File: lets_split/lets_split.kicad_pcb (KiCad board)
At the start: 2 copper layers, 111.8 x 79 mm, 69 parts, among them J1 3PIN, J2 6PIN, J3 3PIN, J4 3PIN, J5 3PIN, M1 FIDUCIAL, M2 FIDUCIAL, M3 FIDUCIAL, M4 FIDUCIAL, SW1 SW_PUSH, SW10 SW_PUSH, SW11 SW_PUSH, SW12 SW_PUSH, SW13 SW_PUSH, SW14 SW_PUSH, SW15 SW_PUSH, SW16 SW_PUSH, SW17 SW_PUSH, SW18 SW_PUSH, SW19 SW_PUSH, SW2 SW_PUSH, SW20 SW_PUSH, SW21 SW_PUSH, SW22 SW_PUSH, SW23 SW_PUSH, SW24 SW_PUSH, SW3 SW_PUSH, SW4 SW_PUSH, SW5 SW_PUSH, SW6 SW_PUSH, SW7 SW_PUSH, SW8 SW_PUSH, SW9 SW_PUSH, U1 ProMicro, U2 HOLE, U3 HOLE, U4 HOLE, U5 HOLE

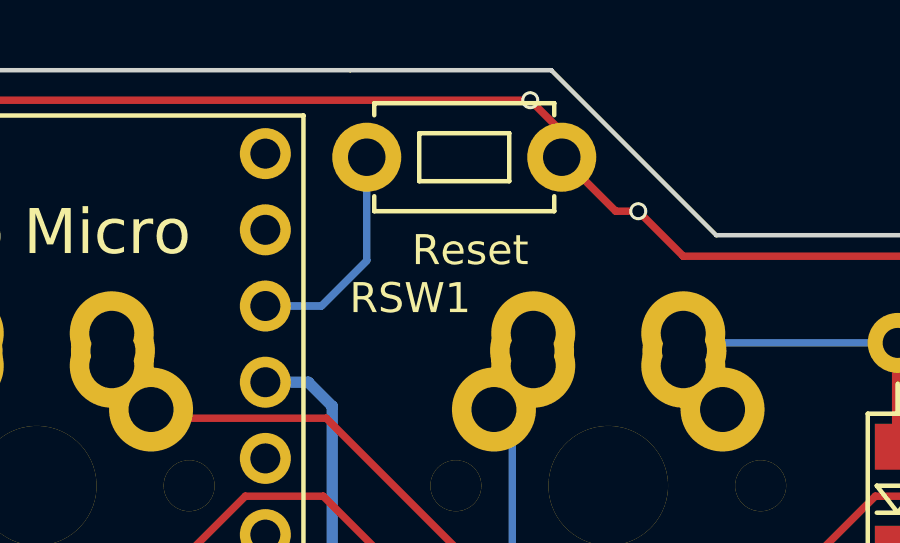
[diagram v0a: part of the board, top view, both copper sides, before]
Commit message: Replace module for reset switch with one compatible to vertical type
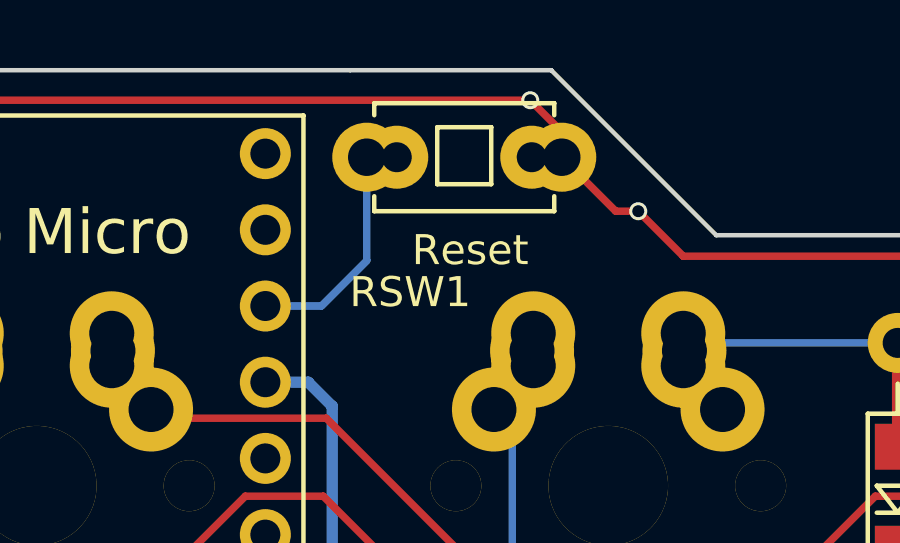
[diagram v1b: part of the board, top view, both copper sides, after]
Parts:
- RSW1: footprint local:SKHL -> local:TACTILE_COMPATIBLE
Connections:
- U1 pad 19: Net-(U1-Pad19) -> (no net)
- U1 pad 2: Net-(U1-Pad2) -> (no net)
- U1 pad 20: Net-(U1-Pad20) -> (no net)
- U1 pad 24: Net-(U1-Pad24) -> (no net)
- U1 pad 7: Net-(U1-Pad7) -> (no net)
- U1 pad 8: Net-(U1-Pad8) -> (no net)
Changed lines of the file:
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@@
     (zones 0)
     (modules 69)
-    (nets 50)
+    (nets 44)
   )
   (page A4)
@@
   (net 42 I2C_SDA)
   (net 43 "Net-(J4-Pad2)")
-  (net 44 "Net-(U1-Pad24)")
-  (net 45 "Net-(U1-Pad20)")
-  (net 46 "Net-(U1-Pad19)")
-  (net 47 "Net-(U1-Pad8)")
-  (net 48 "Net-(U1-Pad7)")
-  (net 49 "Net-(U1-Pad2)")
   (net_class Default "This is the default net class."
     (clearance 0)
@@
     (add_net "Net-(J4-Pad2)")
     (add_net "Net-(RSW1-Pad1)")
-    (add_net "Net-(U1-Pad19)")
-    (add_net "Net-(U1-Pad2)")
-    (add_net "Net-(U1-Pad20)")
-    (add_net "Net-(U1-Pad24)")
-    (add_net "Net-(U1-Pad7)")
-    (add_net "Net-(U1-Pad8)")
     (add_net VCC)
     (add_net col0)
@@
     (add_net row3)
     (add_net xtradata)
+  )
+  (module local:TACTILE_COMPATIBLE (layer F.Cu)
+    (at 78.8 35.9)
+    (fp_text reference RSW1 (at -1.8 4.5) (layer F.SilkS)
+      (effects (font (size 1 1) (thickness 0.15)))
+    )
+    (fp_text value SW_PUSH (at 0 -4.3) (layer F.Fab) hide
+      (effects (font (size 1 1) (thickness 0.15)))
+    )
+    (fp_line (start -0.9 -1) (end 0.9 -1) (layer B.SilkS) (width 0.15))
+    (fp_line (start 0.9 -1) (end 0.9 0.9) (layer B.SilkS) (width 0.15))
+    (fp_line (start 0.9 0.9) (end -0.9 0.9) (layer B.SilkS) (width 0.15))
+    (fp_line (start -0.9 0.9) (end -0.9 -1) (layer B.SilkS) (width 0.15))
+    (fp_line (start -0.9 -1) (end 0.9 -1) (layer F.SilkS) (width 0.15))
+    (fp_line (start 0.9 -1) (end 0.9 0.9) (layer F.SilkS) (width 0.15))
+    (fp_line (start 0.9 0.9) (end -0.9 0.9) (layer F.SilkS) (width 0.15))
+    (fp_line (start -0.9 0.9) (end -0.9 -1) (layer F.SilkS) (width 0.15))
+    (fp_line (start 3 1.3) (end 3 1.8) (layer B.SilkS) (width 0.15))
+    (fp_line (start 3 1.8) (end -3 1.8) (layer B.SilkS) (width 0.15))
+    (fp_line (start -3 1.8) (end -3 1.3) (layer B.SilkS) (width 0.15))
+    (fp_line (start -3 -1.4) (end -3 -1.8) (layer B.SilkS) (width 0.15))
+    (fp_line (start -3 -1.8) (end 3 -1.8) (layer B.SilkS) (width 0.15))
+    (fp_line (start 3 -1.8) (end 3 -1.4) (layer B.SilkS) (width 0.15))
+    (fp_line (start -3 1.8) (end -3 1.3) (layer F.SilkS) (width 0.15))
+    (fp_line (start -3 -1.8) (end -3 -1.4) (layer F.SilkS) (width 0.15))
+    (fp_line (start 3 1.8) (end 3 1.3) (layer F.SilkS) (width 0.15))
+    (fp_line (start 3 -1.8) (end 3 -1.4) (layer F.SilkS) (width 0.15))
+    (fp_line (start -3 1.8) (end 3 1.8) (layer F.SilkS) (width 0.15))
+    (fp_line (start -3 -1.8) (end 3 -1.8) (layer F.SilkS) (width 0.15))
+    (pad 2 thru_hole circle (at 2.25 0) (size 2.1 2.1) (drill 1) (layers *.Cu *.Mask)
+      (net 29 GND))
+    (pad 1 thru_hole circle (at -2.25 0) (size 2.1 2.1) (drill 1) (layers *.Cu *.Mask)
+      (net 41 "Net-(RSW1-Pad1)"))
+    (pad 1 thru_hole circle (at -3.25 0) (size 2.3 2.3) (drill 1.25) (layers *.Cu *.Mask)
+      (net 41 "Net-(RSW1-Pad1)"))
+    (pad 2 thru_hole circle (at 3.25 0) (size 2.3 2.3) (drill 1.25) (layers *.Cu *.Mask)
+      (net 29 GND))
   )
   (module local:MXALPS_FLIP_HOLES (layer F.Cu)
@@
       (effects (font (size 2 1.5) (thickness 0.3)))
     )
-    (pad 24 thru_hole circle (at -13.97 -7.62 270) (size 1.7 1.7) (drill 1) (layers *.Cu *.Mask)
-      (net 44 "Net-(U1-Pad24)"))
+    (pad 24 thru_hole circle (at -13.97 -7.62 270) (size 1.7 1.7) (drill 1) (layers *.Cu *.Mask))
     (pad 23 thru_hole circle (at -11.43 -7.62 270) (size 1.7 1.7) (drill 1) (layers *.Cu *.Mask)
       (net 29 GND))
@@
     (pad 21 thru_hole circle (at -6.35 -7.62 270) (size 1.7 1.7) (drill 1) (layers *.Cu *.Mask)
       (net 31 VCC))
-    (pad 20 thru_hole circle (at -3.81 -7.62 270) (size 1.7 1.7) (drill 1) (layers *.Cu *.Mask)
-      (net 45 "Net-(U1-Pad20)"))
-    (pad 19 thru_hole circle (at -1.27 -7.62 270) (size 1.7 1.7) (drill 1) (layers *.Cu *.Mask)
-      (net 46 "Net-(U1-Pad19)"))
+    (pad 20 thru_hole circle (at -3.81 -7.62 270) (size 1.7 1.7) (drill 1) (layers *.Cu *.Mask))
+    (pad 19 thru_hole circle (at -1.27 -7.62 270) (size 1.7 1.7) (drill 1) (layers *.Cu *.Mask))
     (pad 18 thru_hole circle (at 1.27 -7.62 270) (size 1.7 1.7) (drill 1) (layers *.Cu *.Mask)
       (net 35 col0))
@@
     (pad 9 thru_hole circle (at 6.35 7.62 270) (size 1.7 1.7) (drill 1) (layers *.Cu *.Mask)
       (net 2 row0))
-    (pad 8 thru_hole circle (at 3.81 7.62 270) (size 1.7 1.7) (drill 1) (layers *.Cu *.Mask)
-      (net 47 "Net-(U1-Pad8)"))
-    (pad 7 thru_hole circle (at 1.27 7.62 270) (size 1.7 1.7) (drill 1) (layers *.Cu *.Mask)
-      (net 48 "Net-(U1-Pad7)"))
+    (pad 8 thru_hole circle (at 3.81 7.62 270) (size 1.7 1.7) (drill 1) (layers *.Cu *.Mask))
+    (pad 7 thru_hole circle (at 1.27 7.62 270) (size 1.7 1.7) (drill 1) (layers *.Cu *.Mask))
     (pad 6 thru_hole circle (at -1.27 7.62 270) (size 1.7 1.7) (drill 1) (layers *.Cu *.Mask)
       (net 32 data))
@@
     (pad 3 thru_hole circle (at -8.89 7.62 270) (size 1.7 1.7) (drill 1) (layers *.Cu *.Mask)
       (net 29 GND))
-    (pad 2 thru_hole circle (at -11.43 7.62 270) (size 1.7 1.7) (drill 1) (layers *.Cu *.Mask)
-      (net 49 "Net-(U1-Pad2)"))
+    (pad 2 thru_hole circle (at -11.43 7.62 270) (size 1.7 1.7) (drill 1) (layers *.Cu *.Mask))
     (pad 1 thru_hole rect (at -13.97 7.62 270) (size 1.7 1.7) (drill 1) (layers *.Cu *.Mask)
       (net 43 "Net-(J4-Pad2)"))
   )
-  (module local:SKHL (layer F.Cu)
-    (at 78.8 35.9)
-    (fp_text reference RSW1 (at -1.8 4.7) (layer F.SilkS)
-      (effects (font (size 1 1) (thickness 0.15)))
-    )
-    (fp_text value SW_PUSH (at 0 -4.3) (layer F.Fab) hide
-      (effects (font (size 1 1) (thickness 0.15)))
-    )
-    (fp_line (start -1.5 -0.8) (end 1.5 -0.8) (layer B.SilkS) (width 0.15))
-    (fp_line (start 1.5 -0.8) (end 1.5 0.8) (layer B.SilkS) (width 0.15))
-    (fp_line (start 1.5 0.8) (end -1.5 0.8) (layer B.SilkS) (width 0.15))
-    (fp_line (start -1.5 0.8) (end -1.5 -0.8) (layer B.SilkS) (width 0.15))
-    (fp_line (start 3 1.3) (end 3 1.8) (layer B.SilkS) (width 0.15))
-    (fp_line (start 3 1.8) (end -3 1.8) (layer B.SilkS) (width 0.15))
-    (fp_line (start -3 1.8) (end -3 1.3) (layer B.SilkS) (width 0.15))
-    (fp_line (start -3 -1.4) (end -3 -1.8) (layer B.SilkS) (width 0.15))
-    (fp_line (start -3 -1.8) (end 3 -1.8) (layer B.SilkS) (width 0.15))
-    (fp_line (start 3 -1.8) (end 3 -1.4) (layer B.SilkS) (width 0.15))
-    (fp_line (start -3 1.8) (end -3 1.3) (layer F.SilkS) (width 0.15))
-    (fp_line (start -3 -1.8) (end -3 -1.4) (layer F.SilkS) (width 0.15))
-    (fp_line (start 3 1.8) (end 3 1.3) (layer F.SilkS) (width 0.15))
-    (fp_line (start 3 -1.8) (end 3 -1.4) (layer F.SilkS) (width 0.15))
-    (fp_line (start -1.5 -0.8) (end 1.5 -0.8) (layer F.SilkS) (width 0.15))
-    (fp_line (start 1.5 -0.8) (end 1.5 0.8) (layer F.SilkS) (width 0.15))
-    (fp_line (start 1.5 0.8) (end -1.5 0.8) (layer F.SilkS) (width 0.15))
-    (fp_line (start -1.5 0.8) (end -1.5 -0.8) (layer F.SilkS) (width 0.15))
-    (fp_line (start -3 1.8) (end 3 1.8) (layer F.SilkS) (width 0.15))
-    (fp_line (start -3 -1.8) (end 3 -1.8) (layer F.SilkS) (width 0.15))
-    (pad 1 thru_hole circle (at -3.25 0) (size 2.3 2.3) (drill 1.25) (layers *.Cu *.Mask)
-      (net 41 "Net-(RSW1-Pad1)"))
-    (pad 2 thru_hole circle (at 3.25 0) (size 2.3 2.3) (drill 1.25) (layers *.Cu *.Mask)
-      (net 29 GND))
-  )
   (module local:RESISTOR (layer B.Cu)
